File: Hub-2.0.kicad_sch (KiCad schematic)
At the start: 3 parts, among them SW1 SW_Push_Open, SW2 SW_Push_Open

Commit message: SCH Save
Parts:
- NT1: footprint (none) -> NetTie:NetTie-2_SMD_Pad0.5mm
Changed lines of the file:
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@@
 			)
 		)
-		(property "Footprint" ""
+		(property "Footprint" "NetTie:NetTie-2_SMD_Pad0.5mm"
 			(at 245.11 26.67 0)
 			(hide yes)

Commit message: Mapping for M130, cleanup on all sheets, layout start
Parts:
- removed NT1: NetTie_2, NetTie:NetTie-2_SMD_Pad0.5mm, symbol Device:NetTie_2
- removed SW1, SW2: SW_Push_Open, symbol Switch:SW_Push_Open

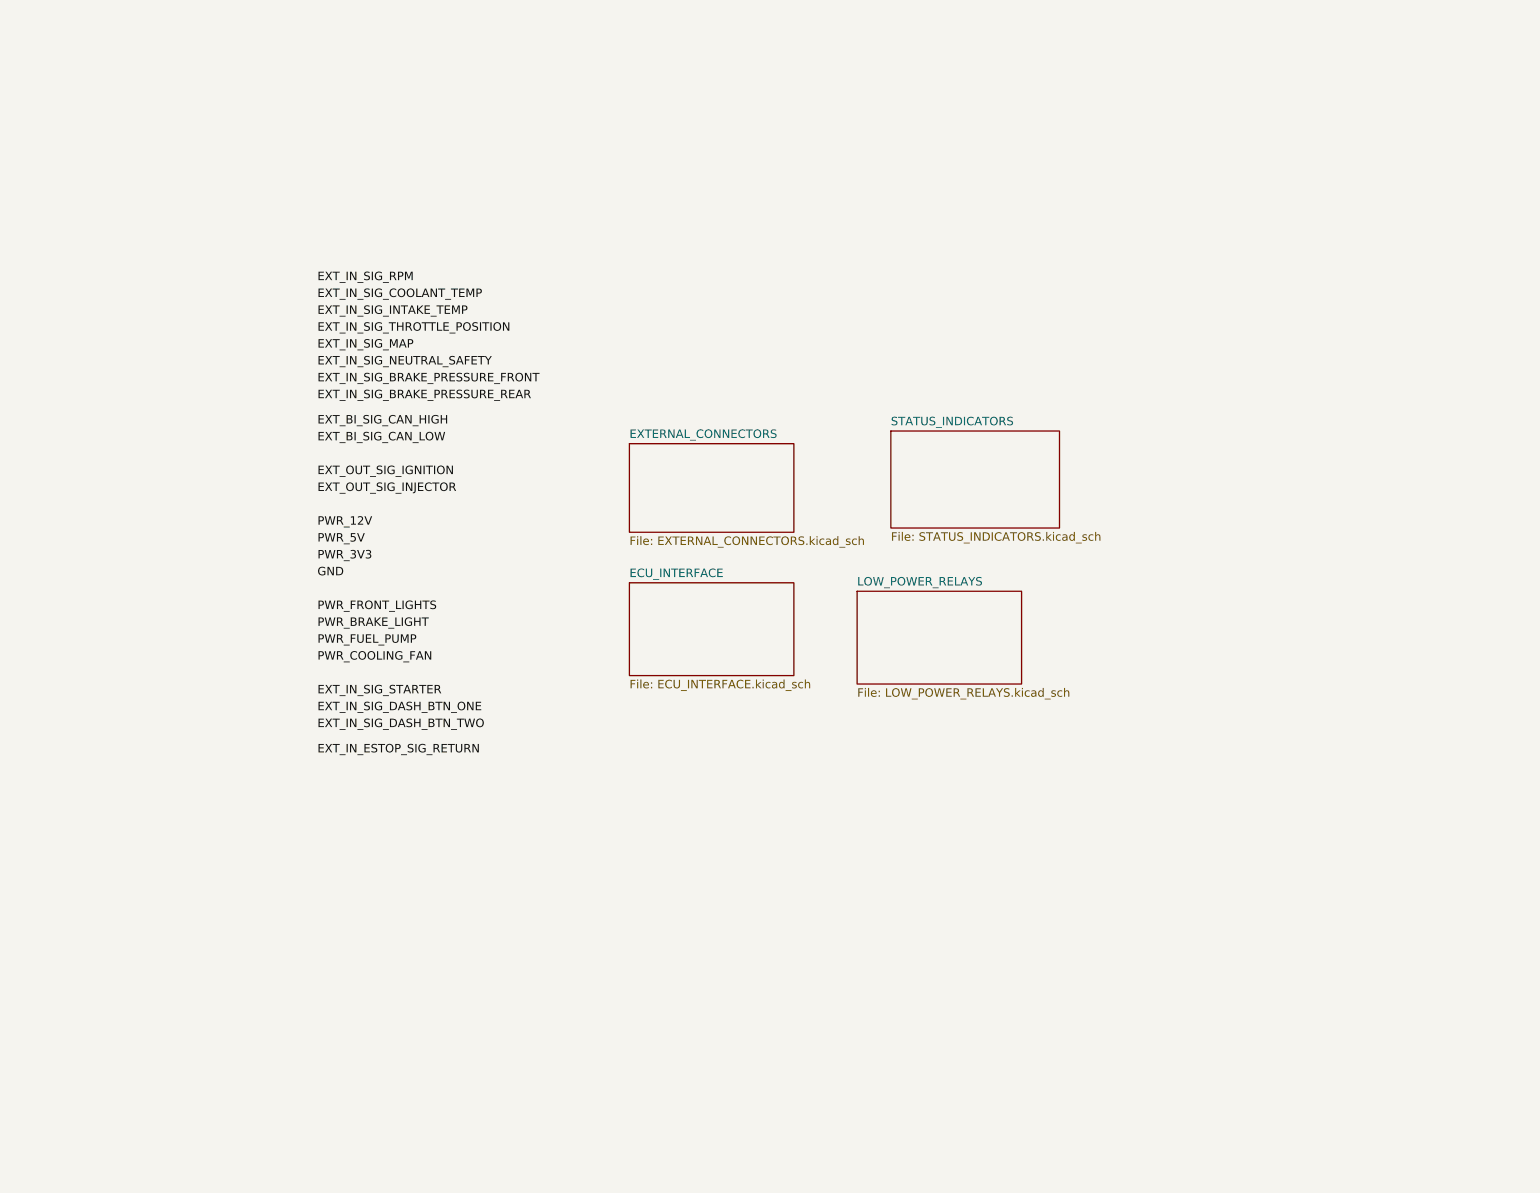
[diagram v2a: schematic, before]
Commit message: Clean up root sheet
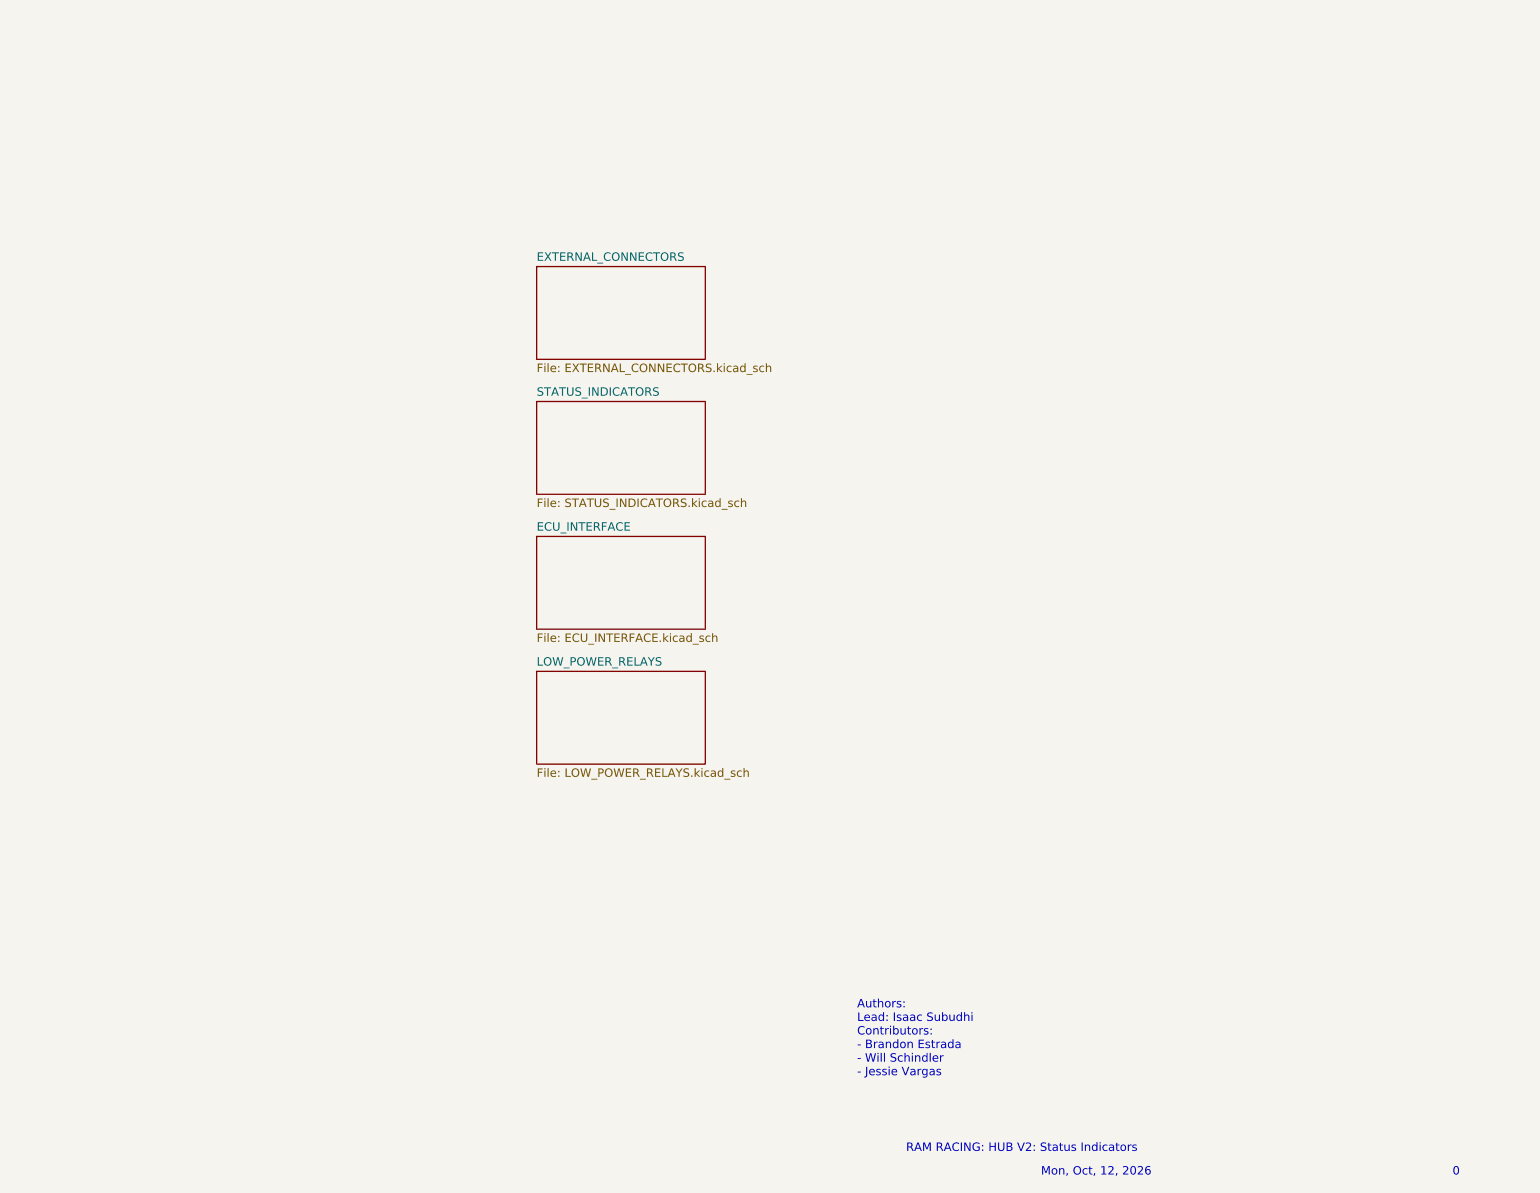
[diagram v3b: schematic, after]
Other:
- note added: "0"
- note added: "Authors: Lead: Isaac Subudhi Contributors: - Brandon Estrada - Will Schindler - Jessie Vargas"
- note added: "Mon, Oct, 12, 2026"
- note added: "RAM RACING: HUB V2: Status Indicators"
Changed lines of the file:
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@@
 	(generator_version "10.0")
 	(paper "A4")
-	(label "GND"
-		(at 96.52 104.14 0)
-		(effects
-			(font
-				(size 1.27 1.27)
-			)
-			(justify left bottom)
-		)
-	)
-	(label "EXT_IN_SIG_BRAKE_PRESSURE_REAR"
-		(at 96.52 77.47 0)
-		(effects
-			(font
-				(size 1.27 1.27)
-			)
-			(justify left bottom)
-		)
-	)
-	(label "EXT_IN_SIG_STARTER"
-		(at 96.52 121.92 0)
-		(effects
-			(font
-				(size 1.27 1.27)
-			)
-			(justify left bottom)
-		)
-	)
-	(label "EXT_BI_SIG_CAN_HIGH"
-		(at 96.52 81.28 0)
-		(effects
-			(font
-				(size 1.27 1.27)
-			)
-			(justify left bottom)
-		)
-	)
-	(label "PWR_3V3"
-		(at 96.52 101.6 0)
-		(effects
-			(font
-				(size 1.27 1.27)
-			)
-			(justify left bottom)
-		)
-	)
-	(label "EXT_IN_SIG_DASH_BTN_TWO"
-		(at 96.52 127 0)
-		(effects
-			(font
-				(size 1.27 1.27)
-			)
-			(justify left bottom)
-		)
-	)
-	(label "PWR_FRONT_LIGHTS"
-		(at 96.52 109.22 0)
-		(effects
-			(font
-				(size 1.27 1.27)
-			)
-			(justify left bottom)
-		)
-	)
-	(label "EXT_IN_SIG_INTAKE_TEMP"
-		(at 96.52 64.77 0)
-		(effects
-			(font
-				(size 1.27 1.27)
-			)
-			(justify left bottom)
-		)
-	)
-	(label "EXT_IN_SIG_COOLANT_TEMP"
-		(at 96.52 62.23 0)
-		(effects
-			(font
-				(size 1.27 1.27)
-			)
-			(justify left bottom)
-		)
-	)
-	(label "EXT_OUT_SIG_INJECTOR"
-		(at 96.52 91.44 0)
-		(effects
-			(font
-				(size 1.27 1.27)
-			)
-			(justify left bottom)
-		)
-	)
-	(label "EXT_IN_ESTOP_SIG_RETURN"
-		(at 96.52 130.81 0)
-		(effects
-			(font
-				(size 1.27 1.27)
-			)
-			(justify left bottom)
-		)
-	)
-	(label "EXT_BI_SIG_CAN_LOW"
-		(at 96.52 83.82 0)
-		(effects
-			(font
-				(size 1.27 1.27)
-			)
-			(justify left bottom)
-		)
-	)
-	(label "EXT_IN_SIG_BRAKE_PRESSURE_FRONT"
-		(at 96.52 74.93 0)
-		(effects
-			(font
-				(size 1.27 1.27)
-			)
-			(justify left bottom)
-		)
-	)
-	(label "EXT_IN_SIG_MAP"
-		(at 96.52 69.85 0)
-		(effects
-			(font
-				(size 1.27 1.27)
-			)
-			(justify left bottom)
-		)
-	)
-	(label "PWR_FUEL_PUMP"
-		(at 96.52 114.3 0)
-		(effects
-			(font
-				(size 1.27 1.27)
-			)
-			(justify left bottom)
-		)
-	)
-	(label "PWR_BRAKE_LIGHT"
-		(at 96.52 111.76 0)
-		(effects
-			(font
-				(size 1.27 1.27)
-			)
-			(justify left bottom)
-		)
-	)
-	(label "EXT_IN_SIG_THROTTLE_POSITION"
-		(at 96.52 67.31 0)
-		(effects
-			(font
-				(size 1.27 1.27)
-			)
-			(justify left bottom)
-		)
-	)
-	(label "EXT_OUT_SIG_IGNITION"
-		(at 96.52 88.9 0)
-		(effects
-			(font
-				(size 1.27 1.27)
-			)
-			(justify left bottom)
-		)
-	)
-	(label "EXT_IN_SIG_RPM"
-		(at 96.52 59.69 0)
-		(effects
-			(font
-				(size 1.27 1.27)
-			)
-			(justify left bottom)
-		)
-	)
-	(label "EXT_IN_SIG_NEUTRAL_SAFETY"
-		(at 96.52 72.39 0)
-		(effects
-			(font
-				(size 1.27 1.27)
-			)
-			(justify left bottom)
-		)
-	)
-	(label "PWR_5V"
-		(at 96.52 99.06 0)
-		(effects
-			(font
-				(size 1.27 1.27)
-			)
-			(justify left bottom)
-		)
-	)
-	(label "PWR_12V"
-		(at 96.52 96.52 0)
-		(effects
-			(font
-				(size 1.27 1.27)
-			)
-			(justify left bottom)
-		)
-	)
-	(label "EXT_IN_SIG_DASH_BTN_ONE"
-		(at 96.52 124.46 0)
-		(effects
-			(font
-				(size 1.27 1.27)
-			)
-			(justify left bottom)
-		)
-	)
-	(label "PWR_COOLING_FAN"
-		(at 96.52 116.84 0)
-		(effects
-			(font
-				(size 1.27 1.27)
-			)
-			(justify left bottom)
-		)
-	)
-	(sheet
-		(at 143.51 104.775)
-		(size 24.765 13.97)
+	(text "Authors: \nLead: Isaac Subudhi\nContributors:\n- Brandon Estrada\n- Will Schindler\n- Jessie Vargas"
+		(exclude_from_sim no)
+		(at 177.8 173.482 0)
+		(effects
+			(font
+				(size 1.27 1.27)
+			)
+			(justify left)
+		)
+	)
+	(text "RAM RACING: HUB V2: Status Indicators"
+		(exclude_from_sim no)
+		(at 185.166 189.992 0)
+		(effects
+			(font
+				(size 1.27 1.27)
+			)
+			(justify left)
+		)
+	)
+	(text "Mon, Oct, 12, 2026\n"
+		(exclude_from_sim no)
+		(at 205.486 193.548 0)
+		(effects
+			(font
+				(size 1.27 1.27)
+			)
+			(justify left)
+		)
+	)
+	(text "0"
+		(exclude_from_sim no)
+		(at 267.462 193.548 0)
+		(effects
+			(font
+				(size 1.27 1.27)
+			)
+			(justify left)
+		)
+	)
+	(sheet
+		(at 129.54 97.79)
+		(size 25.4 13.97)
 		(exclude_from_sim no)
 		(in_bom yes)
@@
 		)
 		(property "Sheetname" "ECU_INTERFACE"
-			(at 143.51 104.0634 0)
+			(at 129.54 97.0784 0)
 			(show_name no)
 			(do_not_autoplace no)
@@
 		)
 		(property "Sheetfile" "ECU_INTERFACE.kicad_sch"
-			(at 143.51 119.3296 0)
+			(at 129.54 112.3446 0)
 			(show_name no)
 			(do_not_autoplace no)
@@
 	)
 	(sheet
-		(at 177.8 106.045)
-		(size 24.765 13.97)
+		(at 129.54 118.11)
+		(size 25.4 13.97)
 		(exclude_from_sim no)
 		(in_bom yes)
@@
 		)
 		(property "Sheetname" "LOW_POWER_RELAYS"
-			(at 177.8 105.3334 0)
+			(at 129.54 117.3984 0)
 			(show_name no)
 			(do_not_autoplace no)
@@
 		)
 		(property "Sheetfile" "LOW_POWER_RELAYS.kicad_sch"
-			(at 177.8 120.5996 0)
+			(at 129.54 132.6646 0)
 			(show_name no)
 			(do_not_autoplace no)
@@
 	)
 	(sheet
-		(at 182.88 81.915)
-		(size 25.4 14.605)
+		(at 129.54 77.47)
+		(size 25.4 13.97)
 		(exclude_from_sim no)
 		(in_bom yes)
@@
 		)
 		(property "Sheetname" "STATUS_INDICATORS"
-			(at 182.88 81.2034 0)
+			(at 129.54 76.7584 0)
 			(show_name no)
 			(do_not_autoplace no)
@@
 		)
 		(property "Sheetfile" "STATUS_INDICATORS.kicad_sch"
-			(at 182.88 97.1046 0)
+			(at 129.54 92.0246 0)
 			(show_name no)
 			(do_not_autoplace no)
@@
 	)
 	(sheet
-		(at 143.51 83.82)
-		(size 24.765 13.335)
+		(at 129.54 57.15)
+		(size 25.4 13.97)
 		(exclude_from_sim no)
 		(in_bom yes)
@@
 		)
 		(property "Sheetname" "EXTERNAL_CONNECTORS"
-			(at 143.51 83.1084 0)
+			(at 129.54 56.4384 0)
 			(show_name no)
 			(do_not_autoplace no)
@@
 		)
 		(property "Sheetfile" "EXTERNAL_CONNECTORS.kicad_sch"
-			(at 143.51 97.7396 0)
-			(show_name no)
-			(do_not_autoplace no)
+			(at 129.54 71.7046 0)
+			(show_name no)
+			(do_not_autoplace no)

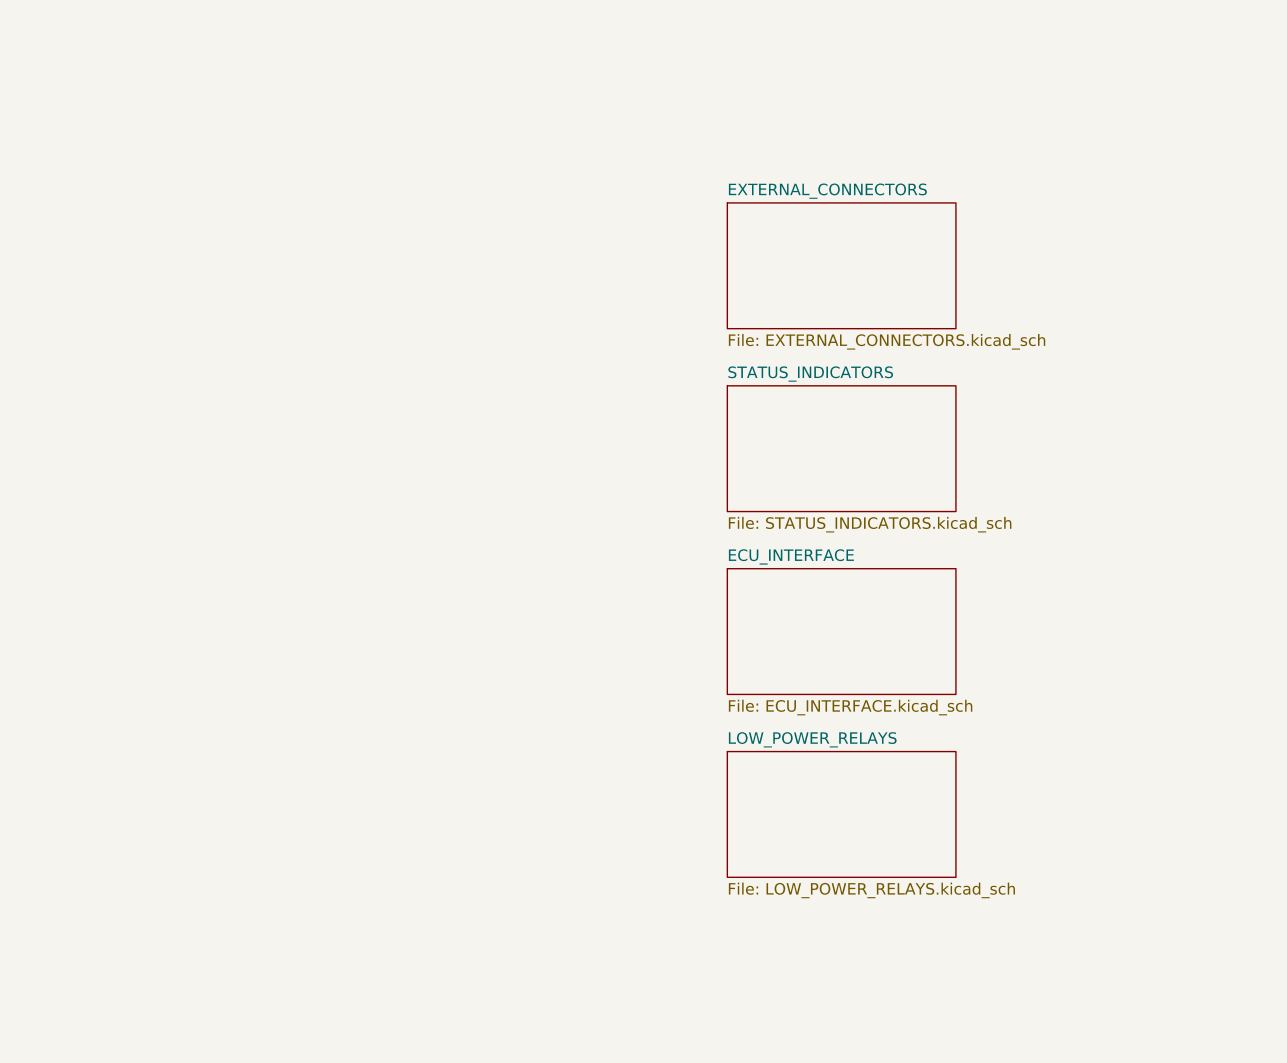
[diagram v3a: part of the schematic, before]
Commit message: Started car wiring sch
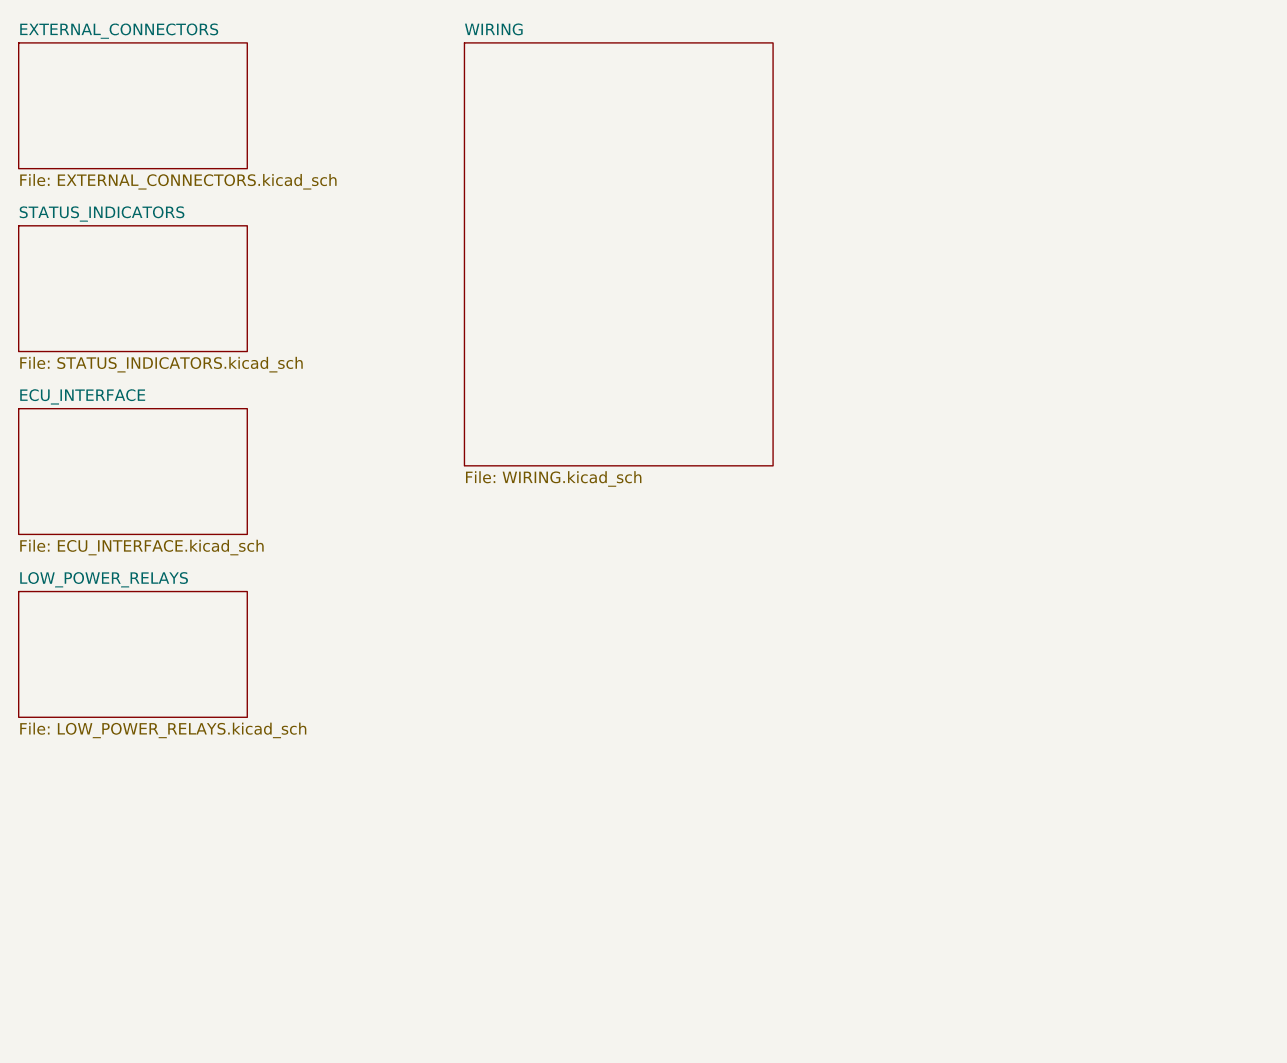
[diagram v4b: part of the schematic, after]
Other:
- added sheet WIRING (WIRING.kicad_sch)
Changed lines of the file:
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@@
 	)
 	(sheet
-		(at 129.54 97.79)
+		(at 100.33 39.37)
+		(size 34.29 46.99)
+		(exclude_from_sim no)
+		(in_bom yes)
+		(on_board yes)
+		(dnp no)
+		(fields_autoplaced yes)
+		(stroke
+			(width 0.1524)
+			(type solid)
+		)
+		(fill
+			(color 0 0 0 0)
+		)
+		(property "Sheetname" "WIRING"
+			(at 100.33 38.6584 0)
+			(show_name no)
+			(do_not_autoplace no)
+			(effects
+				(font
+					(size 1.27 1.27)
+				)
+				(justify left bottom)
+			)
+		)
+		(property "Sheetfile" "WIRING.kicad_sch"
+			(at 100.33 86.9446 0)
+			(show_name no)
+			(do_not_autoplace no)
+			(effects
+				(font
+					(size 1.27 1.27)
+				)
+				(justify left top)
+			)
+		)
+		(instances
+			(project "Hub-2.0"
+				(path "/af8ad92e-80c5-47c7-b528-865d82af0364"
+					(page "6")
+				)
+			)
+		)
+	)
+	(sheet
+		(at 50.8 80.01)
 		(size 25.4 13.97)
 		(exclude_from_sim no)
@@
 		)
 		(property "Sheetname" "ECU_INTERFACE"
-			(at 129.54 97.0784 0)
+			(at 50.8 79.2984 0)
 			(show_name no)
 			(do_not_autoplace no)
@@
 		)
 		(property "Sheetfile" "ECU_INTERFACE.kicad_sch"
-			(at 129.54 112.3446 0)
+			(at 50.8 94.5646 0)
 			(show_name no)
 			(do_not_autoplace no)
@@
 	)
 	(sheet
-		(at 129.54 118.11)
+		(at 50.8 100.33)
 		(size 25.4 13.97)
 		(exclude_from_sim no)
@@
 		)
 		(property "Sheetname" "LOW_POWER_RELAYS"
-			(at 129.54 117.3984 0)
+			(at 50.8 99.6184 0)
 			(show_name no)
 			(do_not_autoplace no)
@@
 		)
 		(property "Sheetfile" "LOW_POWER_RELAYS.kicad_sch"
-			(at 129.54 132.6646 0)
+			(at 50.8 114.8846 0)
 			(show_name no)
 			(do_not_autoplace no)
@@
 	)
 	(sheet
-		(at 129.54 77.47)
+		(at 50.8 59.69)
 		(size 25.4 13.97)
 		(exclude_from_sim no)
@@
 		)
 		(property "Sheetname" "STATUS_INDICATORS"
-			(at 129.54 76.7584 0)
+			(at 50.8 58.9784 0)
 			(show_name no)
 			(do_not_autoplace no)
@@
 		)
 		(property "Sheetfile" "STATUS_INDICATORS.kicad_sch"
-			(at 129.54 92.0246 0)
+			(at 50.8 74.2446 0)
 			(show_name no)
 			(do_not_autoplace no)
@@
 	)
 	(sheet
-		(at 129.54 57.15)
+		(at 50.8 39.37)
 		(size 25.4 13.97)
 		(exclude_from_sim no)
@@
 		)
 		(property "Sheetname" "EXTERNAL_CONNECTORS"
-			(at 129.54 56.4384 0)
+			(at 50.8 38.6584 0)
 			(show_name no)
 			(do_not_autoplace no)
@@
 		)
 		(property "Sheetfile" "EXTERNAL_CONNECTORS.kicad_sch"
-			(at 129.54 71.7046 0)
-			(show_name no)
-			(do_not_autoplace no)
+			(at 50.8 53.9246 0)
+			(show_name no)
+			(do_not_autoplace no)
